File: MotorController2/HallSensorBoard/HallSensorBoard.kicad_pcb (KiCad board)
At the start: 2 copper layers, 6 parts, among them J1 Conn_01x07, J2 Conn_01x02, U1 S49E, U2 S49E, U3 S49E

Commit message: Start on board outline.
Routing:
- net Net-(J1-Pad6): track 0.00 -> 7.71 mm
- net Net-(J1-Pad7): track 0.00 -> 3.55 mm
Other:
- board outline added: 13 x 23 mm
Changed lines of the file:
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@@
   (general
     (thickness 1.6)
-    (drawings 0)
-    (tracks 0)
+    (drawings 4)
+    (tracks 5)
     (zones 0)
     (modules 6)
@@
     )
   )
+  (gr_line (start 148 121) (end 148 98) (layer Edge.Cuts) (width 0.15))
+  (gr_line (start 161 121) (end 148 121) (layer Edge.Cuts) (width 0.15))
+  (gr_line (start 161 98) (end 161 121) (layer Edge.Cuts) (width 0.15))
+  (gr_line (start 148 98) (end 161 98) (layer Edge.Cuts) (width 0.15))
+  (segment (start 153.6 103.45) (end 158.3 103.45) (width 0.25) (layer F.Cu) (net 6))
+  (segment (start 158.3 103.45) (end 159.65 102.1) (width 0.25) (layer F.Cu) (net 6))
+  (segment (start 159.65 102.1) (end 159.65 101) (width 0.25) (layer F.Cu) (net 6))
+  (segment (start 153.6 100.91) (end 157.02 100.91) (width 0.25) (layer F.Cu) (net 7))
+  (segment (start 157.02 100.91) (end 157.11 101) (width 0.25) (layer F.Cu) (net 7))
 )

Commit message: Final board.
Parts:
- added REF**: MountingHole_3.2mm_M3, Mounting_Holes:MountingHole_3.2mm_M3, F.Cu at (156.0, 90.0)
- added REF**: MountingHole_3.2mm_M3, Mounting_Holes:MountingHole_3.2mm_M3, F.Cu at (156.0, 125.0)
- J1, J2: moved to B.Cu
- moved C1 21.4 mm to (158.2, 98.0), turned to 180 degrees
- moved J2 18.2 mm to (155.8, 118.8), turned to 90 degrees
- moved J1 16.3 mm to (153.7, 99.9)
- moved U2 9.61 mm to (158.0, 106.3)
- moved U1 4.03 mm to (158.0, 100.7)
- moved U3 1.65 mm to (158.0, 111.8)
- renumbered U3 to U1, U1 to U3
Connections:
- U1 pad 3: Net-(J1-Pad5) -> Net-(J1-Pad3)
- U3 pad 3: Net-(J1-Pad3) -> Net-(J1-Pad5)
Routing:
- net GND: track 0.00 -> 37.6 mm, vias 0 -> 2
- net +3V3: track 0.00 -> 28.0 mm
- net Net-(J1-Pad5): track 0.00 -> 6.84 mm
- net Net-(J1-Pad3): track 0.00 -> 4.97 mm
- net Net-(J1-Pad4): track 0.00 -> 4.79 mm
- net Net-(J1-Pad6): track 7.71 -> 9.19 mm
- added copper zone on B.Cu, net GND
- added copper zone on F.Cu, net GND
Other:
- board size 13 x 23 mm -> 10 x 43 mm

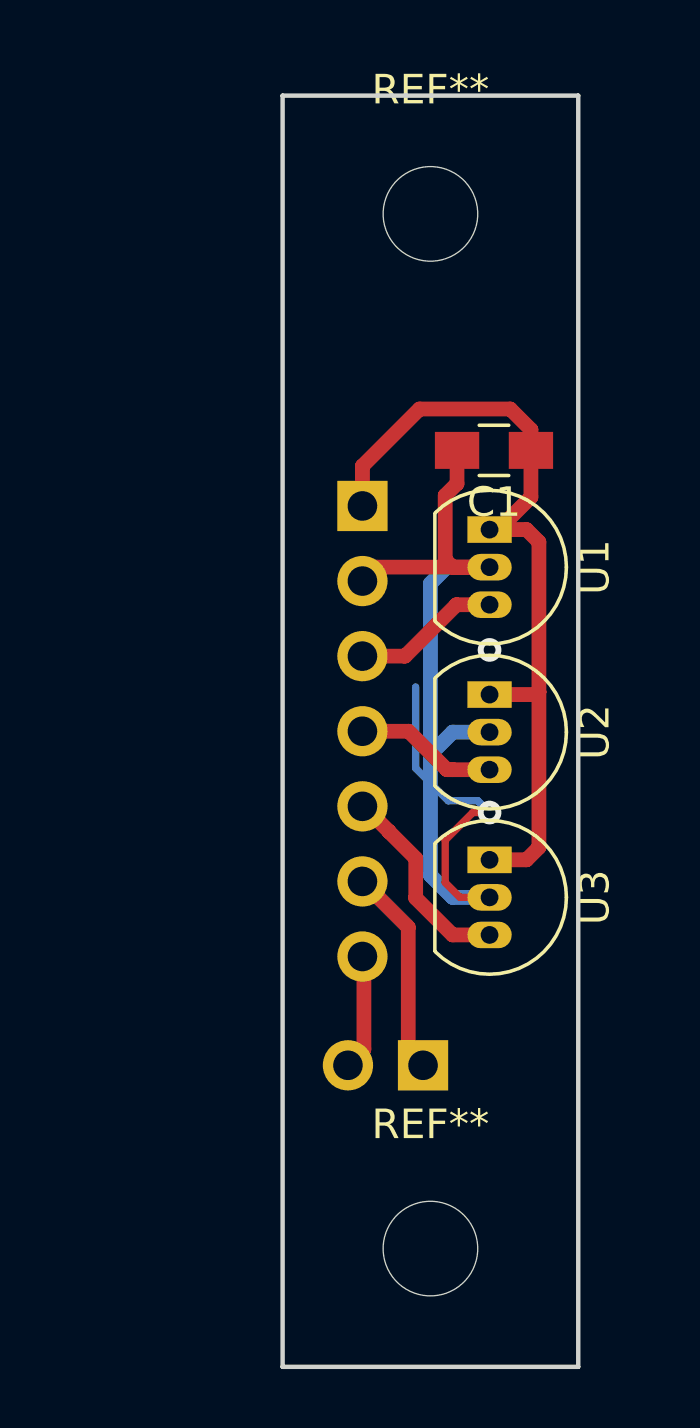
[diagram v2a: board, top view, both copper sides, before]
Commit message: Board layouts as ordered.
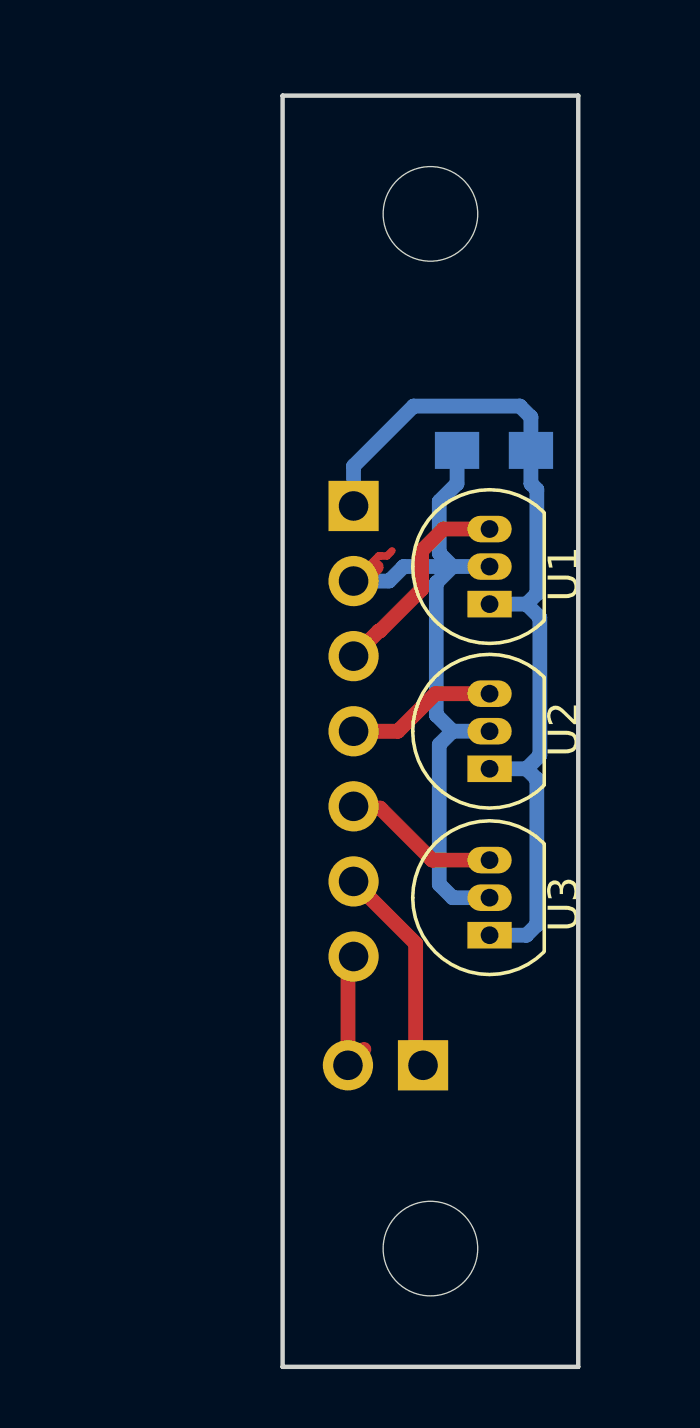
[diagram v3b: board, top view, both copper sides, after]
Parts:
- C1: moved to B.Cu
- moved U3 2.55 mm to (158.0, 114.4), turned to 90 degrees
- moved U1 2.52 mm to (158.0, 103.2), turned to 90 degrees
- moved U2 2.51 mm to (158.0, 108.8), turned to 90 degrees
- moved J1 0.30 mm to (153.4, 99.9)
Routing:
- net GND: track 37.6 -> 26.2 mm, vias 2 -> 0
- net Net-(J1-Pad3): track 4.97 -> 7.74 mm
- net +3V3: track 28.0 -> 30.5 mm
- net Net-(J1-Pad5): track 6.84 -> 5.35 mm
- net Net-(J1-Pad6): track 9.19 -> 7.90 mm
- net Net-(J1-Pad7): track 3.92 -> 4.59 mm
